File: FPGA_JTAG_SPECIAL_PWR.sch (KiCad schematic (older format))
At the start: 44 parts, among them J2 Reset_Switch, U18 LDL212D33R, U19 TLV75512, U900 GW1N-9LQ100

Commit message: Corrected several mistakes in the FPGA symbol, fixed up the FPGA page a little bit.  NOTE: some pin assignments changed position to make reading the schematic easier and to clarify some of the pin functions.
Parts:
- U900: symbol OpenVent:GW1N-9LQ100 -> OpenVent-rescue:GW1N-9LQ100-OpenVent
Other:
- moved on the sheet: U8A
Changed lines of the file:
@@
 $EndComp
 $Comp
-L OpenVent:GW1N-9LQ100 U?
+L OpenVent-rescue:GW1N-9LQ100-OpenVent U?
 U 1 1 5FCF4A75
 P 3725 2825
@@
 AR Path="/5FB692C4/5FCF4A75" Ref="U900"  Part="1"
 AR Path="/5FBE8499/5FCF4A75" Ref="U8"  Part="1"
+AR Path="/5FCF4A75" Ref="U8"  Part="1"
 F 0 "U8" H 4350 4240 50  0000 C CNN
 F 1 "GW1N-9LQ100" H 4350 4149 50  0000 C CNN
@@
 TDO_F
 $Comp
-L OpenVent:GW1N-9LQ100 U?
+L OpenVent-rescue:GW1N-9LQ100-OpenVent U?
 U 2 1 5FB7C2DC
 P 1900 6050
@@
 AR Path="/5FB692C4/5FB7C2DC" Ref="U900"  Part="2"
 AR Path="/5FBE8499/5FB7C2DC" Ref="U8"  Part="2"
+AR Path="/5FB7C2DC" Ref="U8"  Part="2"
 F 0 "U8" H 2825 6715 50  0000 C CNN
 F 1 "GW1N-9LQ100" H 2825 6624 50  0000 C CNN

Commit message: More fixing up of the FPGA symbols, lashed up the sigma delta A/D converter circuitry.  Fixed up the LCD page.  Two displays, two separate enables needed here folks.  FPGA I/O banks power supplies' needs another looking at.  Still lots of stuff to clean up here...
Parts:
- added R31: 12k_0603_Chip_Resistor,_1%,_0.1W, Resistor_SMD:R_0603_1608Metric, symbol OpenVent:12k_0603_Chip_Resistor,_1%,_0.1W
- U900: symbol OpenVent-rescue:GW1N-9LQ100-OpenVent -> OpenVent:GW1N-9LQ100
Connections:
- net +3V3: no longer U900.21 (VCCX)
- net GND: now also R31.1
- net at U900.100 (MODE0): now also R81.2
- net at R29.1, R30.1, U900.54 (VCCX): now also U900.21 (VCCX)
- net JTAGSEL_n: no longer names the net of U900.3 (IOL5A/JTAGSEL_N/LPLL_T_in)
- net JTAGSEL_n: now also R31.2; no longer R81.2
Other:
- note removed: "Pin Number - 54 71 \nGW1N-xV4 LQ100 - Vcco1 Vccx R24, R29\nGW1N-xV9 LQ100 - Vccx Vcco1 R23, R30\n\nPins 54 and 71 are swapped between the -4 and -9 FPGA devices. \n\nAdd R25 and omit R26 when using GW1N-UV device"
- moved on the sheet: R21, R22, R23, R24, R25, R26, R29, R30, U8A

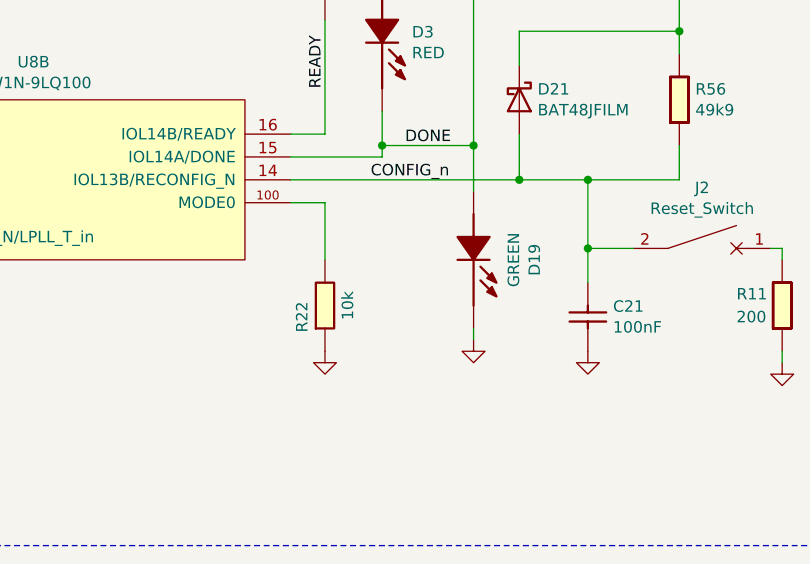
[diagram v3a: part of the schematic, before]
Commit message: Header 2x5 for FPGA was added to JTAG sheet
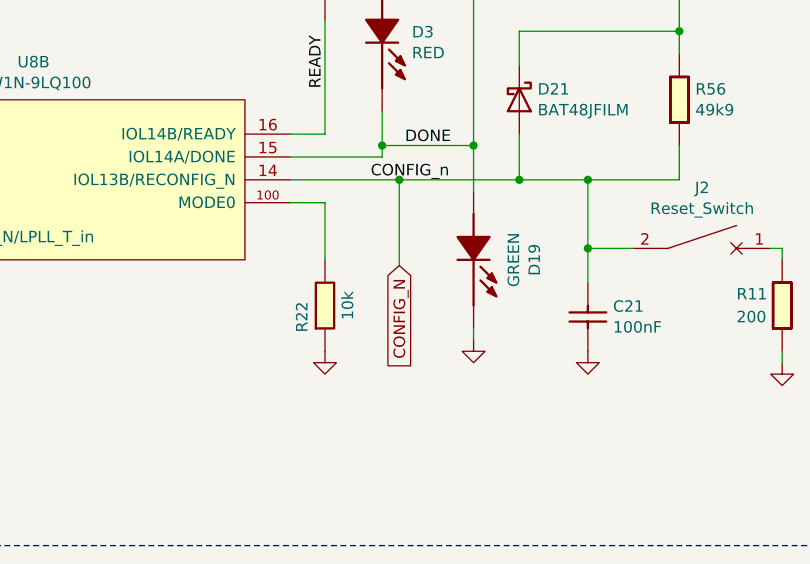
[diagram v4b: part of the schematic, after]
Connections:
- net CONFIG_n renamed CONFIG_N
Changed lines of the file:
@@
 	5050 5900 5050 6200
 Wire Wire Line
-	3750 5900 4750 5900
+	3750 5900 4225 5900
 Wire Wire Line
 	5450 5750 5450 5900
@@
 Wire Wire Line
 	3000 1150 3000 1200
+Wire Wire Line
+	4225 5900 4225 6275
+Connection ~ 4225 5900
+Wire Wire Line
+	4225 5900 4750 5900
+Text GLabel 4225 6275 3    50   Input ~ 0
+CONFIG_N
 $EndSCHEMATC
